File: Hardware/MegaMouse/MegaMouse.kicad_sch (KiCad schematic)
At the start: 14 parts, among them J101 SHIFT_CONN, J102 PROG_CONN, J103 SHIFT_CONN, J104 PROG_CONN

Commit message: Bump config
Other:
- company: (none) -> Kitsune Scientific
- title: (none) -> MegaMouse
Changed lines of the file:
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@@
 (kicad_sch (version 20211123) (generator eeschema)
   (paper "A4")
+  (title_block
+    (title "MegaMouse")
+    (date "${ISSUE}")
+    (rev "${REVISION}")
+    (company "Kitsune Scientific")
+    (comment 4 "Release: ${FULL_REVISION}")
+  )
   (wire (pts (xy 32.385 79.375) (xy 32.385 81.28))
     (stroke (width 0) (type default) (color 0 0 0 0))

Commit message: Awesomeness
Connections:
- net MCU/DATA_OUT: now reaches J103.2 (Pin_2)
- net MCU/LATCH_OUT: now reaches J103.3 (Pin_3)
- net MCU/CLOCK_OUT: now reaches J103.4 (Pin_4)
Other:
- sheet MCU ports: added CLOCK_OUT, DATA_OUT, LATCH_OUT; removed none
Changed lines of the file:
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@@
+      (effects (font (size 1.27 1.27)) (justify left))
+    )
+    (pin "CLOCK_OUT" output (at 134.62 104.14 180)
+      (effects (font (size 1.27 1.27)) (justify left))
+    )
+    (pin "DATA_OUT" output (at 134.62 99.06 180)
+      (effects (font (size 1.27 1.27)) (justify left))
+    )
+    (pin "LATCH_OUT" output (at 134.62 101.6 180)
       (effects (font (size 1.27 1.27)) (justify left))
     )
@@
       (reference "#PWR0412") (unit 1) (value "GND") (footprint "")
     )
-    (path "/078d0145-3523-4341-ae01-8b2b5c73f66a/ce7e64b0-4bb4-482b-abb0-fe1513ed3046"
-      (reference "#PWR0413") (unit 1) (value "GND") (footprint "")
-    )
     (path "/078d0145-3523-4341-ae01-8b2b5c73f66a/9b499c83-7dcf-4728-831a-283f4982f742"
       (reference "#PWR0414") (unit 1) (value "+5V") (footprint "")
     )
-    (path "/078d0145-3523-4341-ae01-8b2b5c73f66a/0d041e25-efa0-49c9-82a3-ae5142e4d930"
-      (reference "#PWR0415") (unit 1) (value "+5V") (footprint "")
-    )
     (path "/0db8d490-e421-418e-81d3-9770b4ca9317/736ccc42-5777-463a-8af5-234b574964de"
       (reference "#PWR0501") (unit 1) (value "GND") (footprint "")
@@
       (reference "#PWR0503") (unit 1) (value "GND") (footprint "")
     )
-    (path "/0db8d490-e421-418e-81d3-9770b4ca9317/70ddc72d-731f-472e-a055-cb8fd5161910"
-      (reference "#PWR0504") (unit 1) (value "GND") (footprint "")
-    )
     (path "/0db8d490-e421-418e-81d3-9770b4ca9317/25c08e8c-098f-4289-adb3-17e47c540648"
       (reference "#PWR0505") (unit 1) (value "GND") (footprint "")
@@
     )
     (path "/078d0145-3523-4341-ae01-8b2b5c73f66a/9cbf446e-0d6d-4b5b-973c-005ac9ffac8f"
-      (reference "C403") (unit 1) (value "22pf") (footprint "Capacitor_SMD:C_0805_2012Metric")
+      (reference "C403") (unit 1) (value "22pf") (footprint "Capacitor_SMD:C_0201_0603Metric")
     )
     (path "/078d0145-3523-4341-ae01-8b2b5c73f66a/8566dc4a-f173-40fa-a76c-b32246aa000b"
-      (reference "C404") (unit 1) (value "22pf") (footprint "Capacitor_SMD:C_0805_2012Metric")
+      (reference "C404") (unit 1) (value "22pf") (footprint "Capacitor_SMD:C_0201_0603Metric")
     )
     (path "/0db8d490-e421-418e-81d3-9770b4ca9317/fc8b80d8-869e-4f21-8470-92310af28bf6"
       (reference "C501") (unit 1) (value "10uf") (footprint "Capacitor_SMD:CP_Elec_4x3")
     )
-    (path "/0db8d490-e421-418e-81d3-9770b4ca9317/bd26693c-cc35-4b74-bbe7-17db26da749c"
-      (reference "C502") (unit 1) (value "100nF") (footprint "Capacitor_SMD:C_0805_2012Metric")
-    )
     (path "/0db8d490-e421-418e-81d3-9770b4ca9317/51e578f6-6872-4182-8932-f41c27ea7c2f"
       (reference "C503") (unit 1) (value "100nF") (footprint "Capacitor_SMD:C_0805_2012Metric")
@@
       (reference "R405") (unit 1) (value "10K") (footprint "Resistor_SMD:R_0805_2012Metric")
     )
-    (path "/078d0145-3523-4341-ae01-8b2b5c73f66a/57ad8578-d30d-4d65-ad7a-ada6249ff7f8"
-      (reference "R406") (unit 1) (value "10K") (footprint "Resistor_SMD:R_0805_2012Metric")
-    )
     (path "/0db8d490-e421-418e-81d3-9770b4ca9317/7e8ea0d0-c0de-441e-9dba-306503ed970f"
       (reference "R501") (unit 1) (value "1K") (footprint "Resistor_SMD:R_0805_2012Metric")
@@
     )
     (path "/078d0145-3523-4341-ae01-8b2b5c73f66a/cd883e07-6a1e-4447-9b7b-5d340c6e8626"
-      (reference "SW402") (unit 1) (value "START_SW") (footprint "Button_Switch_THT:SW_PUSH_6mm_H5mm")
-    )
-    (path "/078d0145-3523-4341-ae01-8b2b5c73f66a/1a5a457f-672e-40cc-b8e9-774174146551"
-      (reference "SW403") (unit 1) (value "STOP/MODE_SW") (footprint "Button_Switch_THT:SW_PUSH_6mm_H5mm")
+      (reference "SW402") (unit 1) (value "START/MODE") (footprint "Button_Switch_THT:SW_Tactile_SKHH_Angled")
     )
     (path "/0db8d490-e421-418e-81d3-9770b4ca9317/f4ecfbab-7766-44c2-87ef-aab75c02cd91"

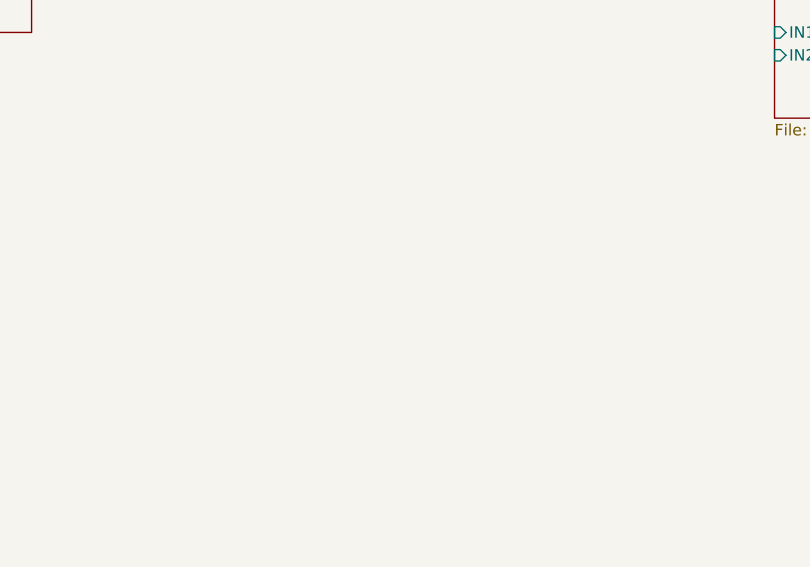
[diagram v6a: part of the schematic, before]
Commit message: Add IR sensor
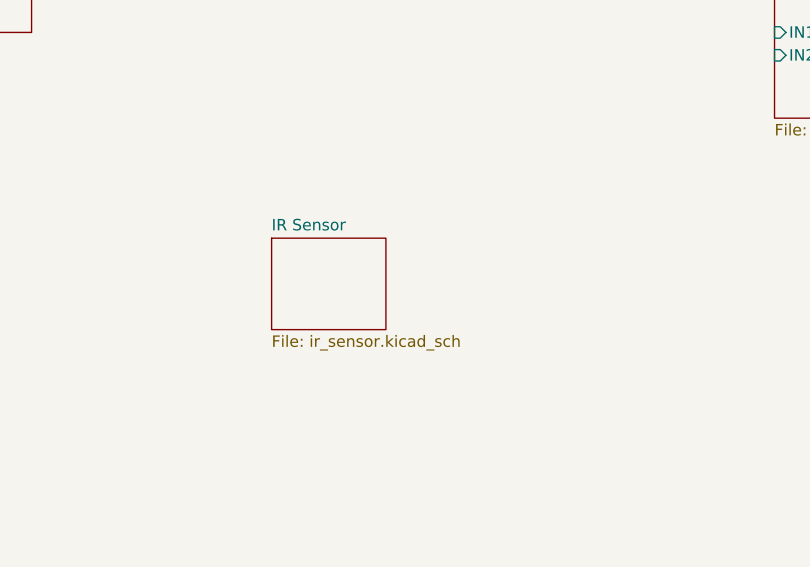
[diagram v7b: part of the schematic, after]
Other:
- added sheet IR Sensor (ir_sensor.kicad_sch)
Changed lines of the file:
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@@
+    )
+  )
+  (sheet (at 193.04 133.985) (size 12.7 10.16) (fields_autoplaced)
+    (stroke (width 0.1524) (type solid) (color 0 0 0 0))
+    (fill (color 0 0 0 0.0000))
+    (property "Sheet name" "IR Sensor" (id 0) (at 193.04 133.2734 0)
+      (effects (font (size 1.27 1.27)) (justify left bottom))
+    )
+    (property "Sheet file" "ir_sensor.kicad_sch" (id 1) (at 193.04 144.7296 0)
+      (effects (font (size 1.27 1.27)) (justify left top))
     )
   )
@@
     (path "/0db8d490-e421-418e-81d3-9770b4ca9317" (page "5"))
     (path "/15cf0a12-7ae2-4a92-a2cb-9d52cdb2502c" (page "6"))
+    (path "/bba3cf1b-7655-42d9-87a8-1fb88711e0bf" (page "7"))
   )
   (symbol_instances
@@
       (reference "D603") (unit 1) (value "TX") (footprint "LED_SMD:LED_0805_2012Metric")
     )
+    (path "/bba3cf1b-7655-42d9-87a8-1fb88711e0bf/f80ac57e-4686-488f-a27c-9c22b045a001"
+      (reference "D701") (unit 1) (value "D_Photo") (footprint "LED_THT:LED_D5.0mm_Horizontal_O1.27mm_Z3.0mm_IRBlack")
+    )
     (path "/6078ab87-f88b-4fb5-bc0e-1362b8855326"
       (reference "H101") (unit 1) (value "MountingHole_Pad") (footprint "MountingHole:MountingHole_3mm_Pad")
@@
       (reference "R608") (unit 1) (value "1K") (footprint "Resistor_SMD:R_0805_2012Metric")
     )
+    (path "/15cf0a12-7ae2-4a92-a2cb-9d52cdb2502c/33f7973f-e682-4b67-ac9a-a68f88488048"
+      (reference "R609") (unit 1) (value "1K") (footprint "Resistor_SMD:R_0805_2012Metric")
+    )
+    (path "/15cf0a12-7ae2-4a92-a2cb-9d52cdb2502c/9e957fa4-4b7d-407f-a815-ccf11d11bf03"
+      (reference "R610") (unit 1) (value "1K") (footprint "Resistor_SMD:R_0805_2012Metric")
+    )
+    (path "/15cf0a12-7ae2-4a92-a2cb-9d52cdb2502c/1cc15f9f-3e9d-4595-8e31-683dae4e6cbb"
+      (reference "R611") (unit 1) (value "1K") (footprint "Resistor_SMD:R_0805_2012Metric")
+    )
+    (path "/15cf0a12-7ae2-4a92-a2cb-9d52cdb2502c/fc3e3068-ff37-4de4-8b8d-40a7f1a95ff1"
+      (reference "R612") (unit 1) (value "1K") (footprint "Resistor_SMD:R_0805_2012Metric")
+    )
+    (path "/15cf0a12-7ae2-4a92-a2cb-9d52cdb2502c/15859273-e25b-4de9-a85d-9be020ccb78d"
+      (reference "R613") (unit 1) (value "1K") (footprint "Resistor_SMD:R_0805_2012Metric")
+    )
+    (path "/15cf0a12-7ae2-4a92-a2cb-9d52cdb2502c/6115708a-096d-4245-818a-81eb209d8b55"
+      (reference "R614") (unit 1) (value "1K") (footprint "Resistor_SMD:R_0805_2012Metric")
+    )
+    (path "/15cf0a12-7ae2-4a92-a2cb-9d52cdb2502c/fcce9388-132c-44cf-8514-259ec884b73f"
+      (reference "R615") (unit 1) (value "1K") (footprint "Resistor_SMD:R_0805_2012Metric")
+    )
+    (path "/15cf0a12-7ae2-4a92-a2cb-9d52cdb2502c/f7bec54b-f80a-459a-9520-d6ae583bd257"
+      (reference "R616") (unit 1) (value "1K") (footprint "Resistor_SMD:R_0805_2012Metric")
+    )
     (path "/078d0145-3523-4341-ae01-8b2b5c73f66a/a7079559-26b6-43bc-86a7-dfee96e5ef94"

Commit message: Add silkscreen!
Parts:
- added JP101: BrakeBridge, Jumper:SolderJumper-2_P1.3mm_Bridged_Pad1.0x1.5mm, symbol Jumper:SolderJumper_2_Bridged
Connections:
- net R_TURN: now reaches R103.2
- net L_TURN: now reaches R101.2
- net BRAKE: now reaches R104.2
- net BRAKE: now also R102.2, JP101.2 (B)
- new net MCU/SCK: JP101.1 (A)
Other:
- sheet MCU ports: added L_TURN, R_TURN, SCK; removed none
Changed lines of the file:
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@@
     (comment 4 "Release: ${FULL_REVISION}")
   )
+  (wire (pts (xy 166.37 99.06) (xy 190.5 99.06))
+    (stroke (width 0) (type default) (color 0 0 0 0))
+  )
   (wire (pts (xy 32.385 79.375) (xy 32.385 81.28))
     (stroke (width 0) (type default) (color 0 0 0 0))
@@
     (stroke (width 0) (type default) (color 0 0 0 0))
   )
+  (wire (pts (xy 190.5 104.14) (xy 180.975 104.14))
+    (stroke (width 0) (type default) (color 0 0 0 0))
+  )
   (wire (pts (xy 32.385 50.165) (xy 32.385 47.625))
     (stroke (width 0) (type default) (color 0 0 0 0))
   )
+  (wire (pts (xy 67.31 50.165) (xy 57.785 50.165))
+    (stroke (width 0) (type default) (color 0 0 0 0))
+  )
   (wire (pts (xy 32.385 38.1) (xy 32.385 35.56))
     (stroke (width 0) (type default) (color 0 0 0 0))
@@
     (stroke (width 0) (type default) (color 0 0 0 0))
   )
+  (wire (pts (xy 190.5 101.6) (xy 166.37 101.6))
+    (stroke (width 0) (type default) (color 0 0 0 0))
+  )
   (wire (pts (xy 123.825 83.185) (xy 123.825 85.09))
     (stroke (width 0) (type default) (color 0 0 0 0))
@@
     (stroke (width 0) (type default) (color 0 0 0 0))
   )
+  (wire (pts (xy 67.31 38.1) (xy 57.785 38.1))
+    (stroke (width 0) (type default) (color 0 0 0 0))
+  )
   (wire (pts (xy 118.745 106.68) (xy 123.19 106.68))
     (stroke (width 0) (type default) (color 0 0 0 0))
@@
     (stroke (width 0) (type default) (color 0 0 0 0))
   )
+  (wire (pts (xy 173.355 104.14) (xy 166.37 104.14))
+    (stroke (width 0) (type default) (color 0 0 0 0))
+  )
   (wire (pts (xy 32.385 35.56) (xy 34.925 35.56))
     (stroke (width 0) (type default) (color 0 0 0 0))
   )
+  (wire (pts (xy 67.31 33.02) (xy 57.785 33.02))
+    (stroke (width 0) (type default) (color 0 0 0 0))
+  )
   (wire (pts (xy 31.75 92.71) (xy 27.305 92.71))
     (stroke (width 0) (type default) (color 0 0 0 0))
@@
   (wire (pts (xy 46.355 190.5) (xy 46.355 192.405))
     (stroke (width 0) (type default) (color 0 0 0 0))
+  )
+  (wire (pts (xy 67.31 45.085) (xy 57.785 45.085))
+    (stroke (width 0) (type default) (color 0 0 0 0))
+  )
+  (label "BRAKE" (at 67.31 50.165 180)
+    (effects (font (size 1.27 1.27)) (justify right bottom))
+  )
+  (label "BRAKE" (at 67.31 38.1 180)
+    (effects (font (size 1.27 1.27)) (justify right bottom))
+  )
+  (label "L_TURN" (at 190.5 101.6 180)
+    (effects (font (size 1.27 1.27)) (justify right bottom))
+  )
+  (label "L_TURN" (at 67.31 33.02 180)
+    (effects (font (size 1.27 1.27)) (justify right bottom))
+  )
+  (label "BRAKE" (at 190.5 104.14 180)
+    (effects (font (size 1.27 1.27)) (justify right bottom))
+  )
+  (label "R_TURN" (at 67.31 45.085 180)
+    (effects (font (size 1.27 1.27)) (justify right bottom))
+  )
+  (label "R_TURN" (at 190.5 99.06 180)
+    (effects (font (size 1.27 1.27)) (justify right bottom))
   )
   (symbol (lib_id "power:GND") (at 123.19 108.585 0) (unit 1)
@@
     (pin "1")
   )
+  (symbol (lib_id "Jumper:SolderJumper_2_Bridged") (at 177.165 104.14 0) (unit 1)
+    (in_bom yes) (on_board yes)
+    (property "Reference" "JP101" (id 0) (at 171.45 102.87 0))
+    (property "Value" "BrakeBridge" (id 1) (at 177.165 100.965 0)
+      (effects (font (size 1.27 1.27)) hide)
+    )
+    (property "Footprint" "Jumper:SolderJumper-2_P1.3mm_Bridged_Pad1.0x1.5mm" (id 2) (at 177.165 104.14 0)
+      (effects (font (size 1.27 1.27)) hide)
+    )
+    (property "Datasheet" "~" (id 3) (at 177.165 104.14 0)
+      (effects (font (size 1.27 1.27)) hide)
+    )
+    (pin "1")
+    (pin "2")
+  )
   (symbol (lib_id "Device:R_Small") (at 55.245 50.165 90) (unit 1)
     (in_bom yes) (on_board yes)
@@
     (pin "LATCH_OUT" output (at 134.62 101.6 180)
       (effects (font (size 1.27 1.27)) (justify left))
+    )
+    (pin "R_TURN" output (at 166.37 99.06 0)
+      (effects (font (size 1.27 1.27)) (justify right))
+    )
+    (pin "L_TURN" output (at 166.37 101.6 0)
+      (effects (font (size 1.27 1.27)) (justify right))
+    )
+    (pin "SCK" output (at 166.37 104.14 0)
+      (effects (font (size 1.27 1.27)) (justify right))
     )
   )
@@
       (reference "#PWR0410") (unit 1) (value "GND") (footprint "")
     )
-    (path "/078d0145-3523-4341-ae01-8b2b5c73f66a/ce3e9335-e654-4be8-b96e-bd29448835ab"
-      (reference "#PWR0411") (unit 1) (value "GND") (footprint "")
-    )
     (path "/078d0145-3523-4341-ae01-8b2b5c73f66a/933c9b18-f744-4e35-b524-c2721b8c48c1"
-      (reference "#PWR0412") (unit 1) (value "+5V") (footprint "")
+      (reference "#PWR0411") (unit 1) (value "+5V") (footprint "")
     )
     (path "/078d0145-3523-4341-ae01-8b2b5c73f66a/91569236-039d-42a2-bb05-f644c7390795"
+      (reference "#PWR0412") (unit 1) (value "GND") (footprint "")
+    )
+    (path "/078d0145-3523-4341-ae01-8b2b5c73f66a/d0a4badf-40d2-4bbb-84c7-0cddfdfcb3b3"
       (reference "#PWR0413") (unit 1) (value "GND") (footprint "")
     )
-    (path "/078d0145-3523-4341-ae01-8b2b5c73f66a/d0a4badf-40d2-4bbb-84c7-0cddfdfcb3b3"
-      (reference "#PWR0414") (unit 1) (value "GND") (footprint "")
-    )
     (path "/078d0145-3523-4341-ae01-8b2b5c73f66a/9b499c83-7dcf-4728-831a-283f4982f742"
-      (reference "#PWR0415") (unit 1) (value "+5V") (footprint "")
+      (reference "#PWR0414") (unit 1) (value "+5V") (footprint "")
     )
     (path "/0db8d490-e421-418e-81d3-9770b4ca9317/736ccc42-5777-463a-8af5-234b574964de"
@@
       (reference "D102") (unit 1) (value "RightTail") (footprint "MegaMouse:BrakeLight")
     )
-    (path "/078d0145-3523-4341-ae01-8b2b5c73f66a/8b4a1ab3-04a2-4c1d-9f67-8fdec242e15f"
-      (reference "D401") (unit 1) (value "STAT") (footprint "LED_SMD:LED_0805_2012Metric")
-    )
     (path "/0db8d490-e421-418e-81d3-9770b4ca9317/91f5a407-d7ba-479a-9083-3037f6c41eef"
       (reference "D501") (unit 1) (value "PWR") (footprint "LED_SMD:LED_0805_2012Metric")
@@
       (reference "J601") (unit 1) (value "USBC") (footprint "Connector_USB:USB_C_Receptacle_XKB_U262-16XN-4BVC11")
     )
+    (path "/de40056f-3bb8-4902-a5a2-f617100b2729"
+      (reference "JP101") (unit 1) (value "BrakeBridge") (footprint "Jumper:SolderJumper-2_P1.3mm_Bridged_Pad1.0x1.5mm")
+    )
     (path "/078d0145-3523-4341-ae01-8b2b5c73f66a/8272bf65-ac58-4265-bbfa-781b0fa0d3e3"
       (reference "JP401") (unit 1) (value "RSTBridge") (footprint "Jumper:SolderJumper-2_P1.3mm_Bridged_Pad1.0x1.5mm")
@@
       (reference "R402") (unit 1) (value "1K") (footprint "Resistor_SMD:R_0805_2012Metric")
     )
-    (path "/078d0145-3523-4341-ae01-8b2b5c73f66a/3ce00995-0565-4e80-ab47-8de755fcedbc"
+    (path "/078d0145-3523-4341-ae01-8b2b5c73f66a/70d215ad-7fe4-43ad-9cda-3f9fe39c67d6"
       (reference "R403") (unit 1) (value "1K") (footprint "Resistor_SMD:R_0805_2012Metric")
     )
-    (path "/078d0145-3523-4341-ae01-8b2b5c73f66a/70d215ad-7fe4-43ad-9cda-3f9fe39c67d6"
-      (reference "R404") (unit 1) (value "1K") (footprint "Resistor_SMD:R_0805_2012Metric")
-    )
     (path "/078d0145-3523-4341-ae01-8b2b5c73f66a/b18a39b4-7f48-40a4-9211-b5f89d42f33a"
-      (reference "R405") (unit 1) (value "10K") (footprint "Resistor_SMD:R_0805_2012Metric")
+      (reference "R404") (unit 1) (value "10K") (footprint "Resistor_SMD:R_0805_2012Metric")
     )
     (path "/0db8d490-e421-418e-81d3-9770b4ca9317/7e8ea0d0-c0de-441e-9dba-306503ed970f"
